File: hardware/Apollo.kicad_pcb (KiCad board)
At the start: 2 copper layers, 101.2 x 199.1 mm, 82 parts, among them J1 TYPE-C 16PIN 2MD(073), J2 Conn_ARM_JTAG_SWD_10, J22 Conn_01x16, J3 Conn_02x03_Odd_Even, J4 Conn_02x04_Odd_Even, Q1 DMP1045U-7, Q2 SS8550, Q3 SS8050, Q4 SS8050, Q5 SL1254-3, SW1 MK-12C01-G1.5, SW2 TS-1095PS-A1B2-C3D2, SW3 TS-1095PS-A1B2-C3D2, SW4 10*10*9-6P WX, U1 TPS63031DSK, U10 PY25Q128HA, U11 SAINTCON-Minibadge, U12 SAINTCON-Minibadge, U2 RP2350A-QFN60, U3 SAINTCON-Minibadge, U4 SAINTCON-Minibadge, U5 SAINTCON-Minibadge, U6 SAINTCON-Minibadge, U7 24CS02, U8 SAINTCON-Minibadge, U9 SAINTCON-Minibadge, Y1 12Mhz

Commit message: prototype v0.3
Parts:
- removed SW4: 10*10*9-6P WX, easyeda2kicad:SW-SMD-6P-L10.5-W10.0_C2858290
- added SW5: 7*7*5-6P-L WX, easyeda2kicad:SW-SMD_8P-L7.0-W7.0-P1.40-LS7.4-TL, F.Cu at (112.7, 172.2)
- added TP4: TestPoint, TestPoint:TestPoint_Pad_D1.0mm, B.Cu at (166.6, 173.2)
- added TP5: TestPoint, TestPoint:TestPoint_Pad_D1.0mm, B.Cu at (122.0, 173.0)
- C14: value 0.1uF -> 100nF
- moved TP2 13.2 mm to (176.6, 168.0)
- moved TP1 13.2 mm to (174.0, 168.0)
- moved TP3 13.2 mm to (171.4, 168.0)
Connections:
- U2 pad 31: JOY_B -> JOY_L
- U2 pad 33: JOY_U -> JOY_B
- U2 pad 35: JOY_L -> JOY_U
- U2 pad 43: unconnected-(U2-GPIO29_ADC3-Pad43) -> Net-(U2-GPIO29_ADC3)
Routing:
- net Net-(U2-GPIO29_ADC3): track 0.00 -> 91.3 mm, vias 0 -> 2
- net +3.3V: track 841.1 -> 805.7 mm
- net JOY_D: track 104.8 -> 96.8 mm
- net TX: track 170.9 -> 174.1 mm
- net JOY_B: track 93.1 -> 96.0 mm
- net Net-(D5-DOUT): track 47.7 -> 50.1 mm
- net JOY_U: track 101.2 -> 99.1 mm
- net BTN2: track 121.7 -> 120.3 mm
- net Net-(D7-DOUT): track 49.8 -> 48.4 mm
- net JOY_R: track 96.0 -> 94.9 mm
- net 1HZ_CLK: track 201.6 -> 202.3 mm
- net SCL: track 225.6 -> 226.1 mm
- net SDA: track 225.8 -> 226.3 mm
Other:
- board text removed: "SAINTCON"

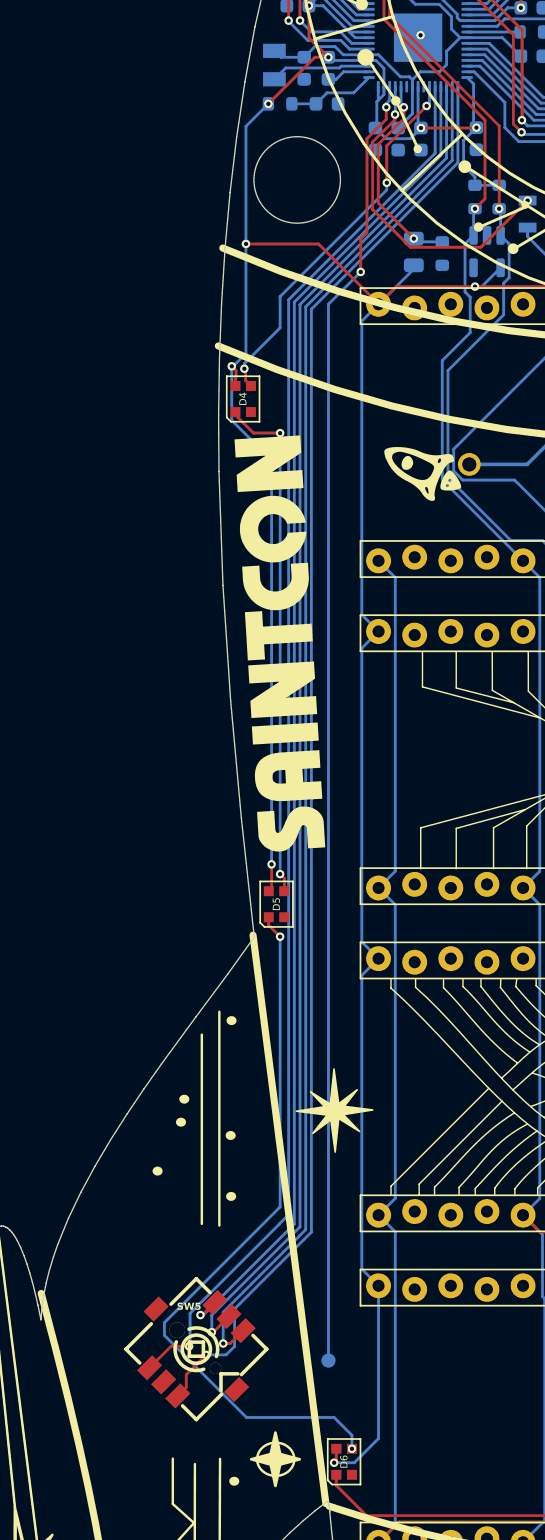
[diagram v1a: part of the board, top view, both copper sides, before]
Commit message: Updated joystick
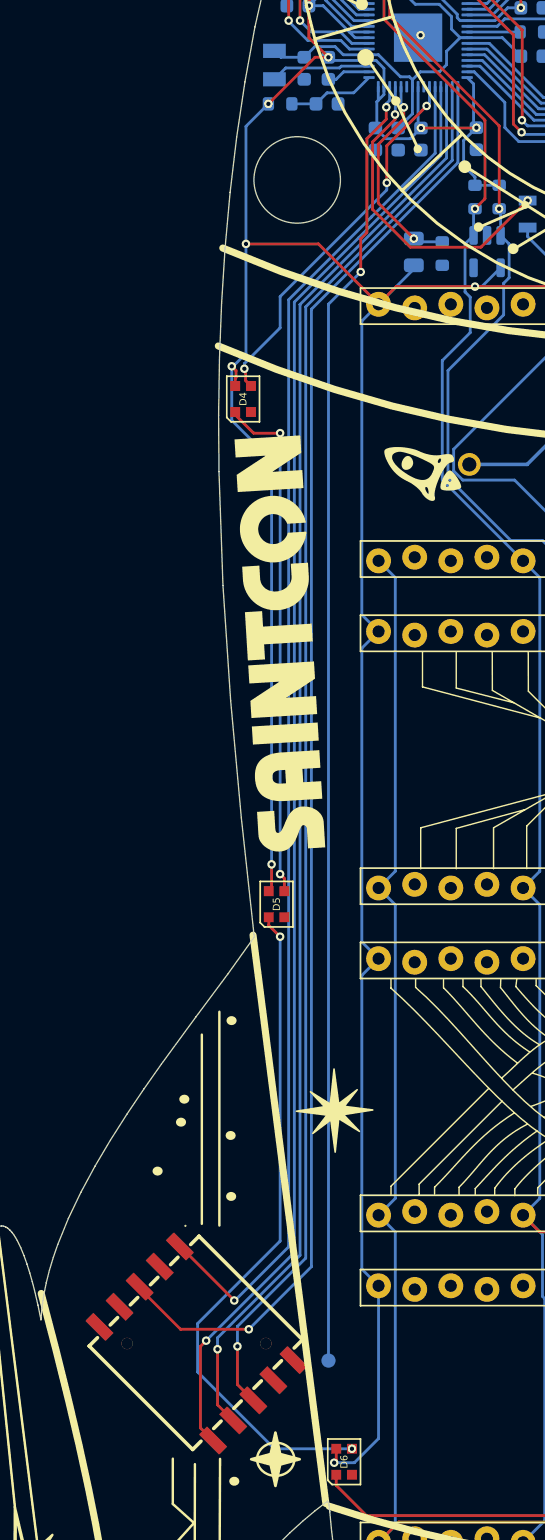
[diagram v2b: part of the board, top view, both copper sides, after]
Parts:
- removed SW5: 7*7*5-6P-L WX, easyeda2kicad:SW-SMD_8P-L7.0-W7.0-P1.40-LS7.4-TL
- added SW4: K1-1507SA-03, easyeda2kicad:KEY-SMD_K1-1507SA-03, F.Cu at (112.7, 171.8)
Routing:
- net JOY_R: track 94.9 -> 102.5 mm
- net JOY_B: track 96.0 -> 100.9 mm
- net JOY_U: track 99.1 -> 96.6 mm
- net Net-(D5-DOUT): track 50.1 -> 47.8 mm
- net JOY_D: track 96.8 -> 99.1 mm
- net JOY_L: track 101.0 -> 102.4 mm

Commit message: accel added
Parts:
- added C23: 1uF, Capacitor_SMD:C_0603_1608Metric, B.Cu at (139.0, 89.4)
- added C24: 100nF, Capacitor_SMD:C_0603_1608Metric, B.Cu at (140.8, 89.4)
- added U13: STK8321, Package_LGA:LGA-12_2x2mm_P0.5mm, B.Cu at (136.4, 89.2)
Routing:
- net +3.3V: track 805.7 -> 821.5 mm, vias 24 -> 27
- net SCL: track 226.1 -> 231.1 mm
- net GND: track 18.4 -> 20.3 mm, vias 5 -> 7
- net SDA: track 226.3 -> 228.0 mm, vias 2 -> 3

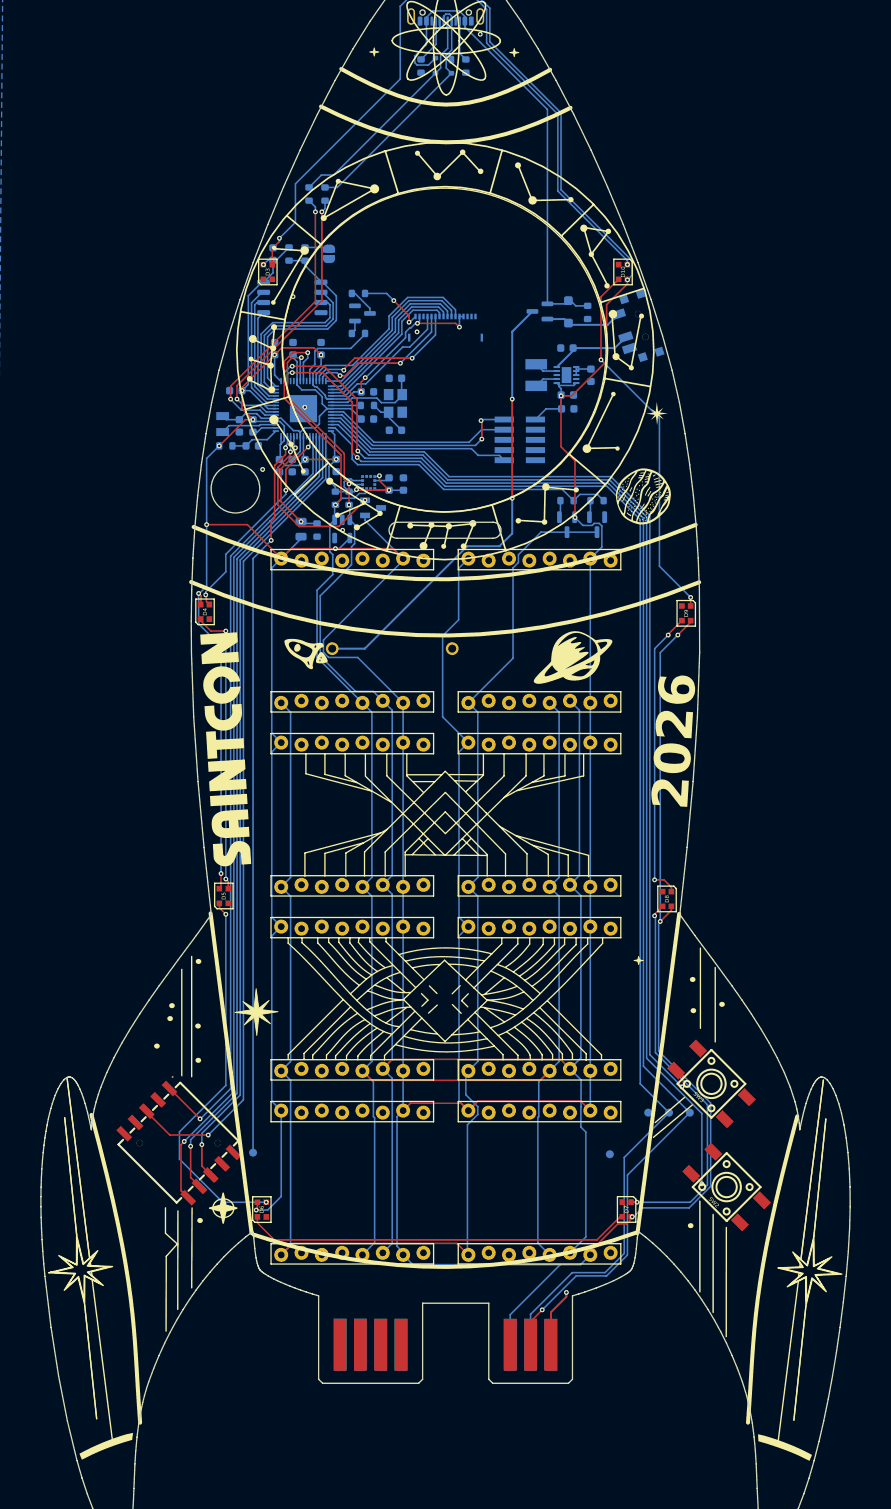
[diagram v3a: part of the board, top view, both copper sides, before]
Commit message: Restoring Orion trail
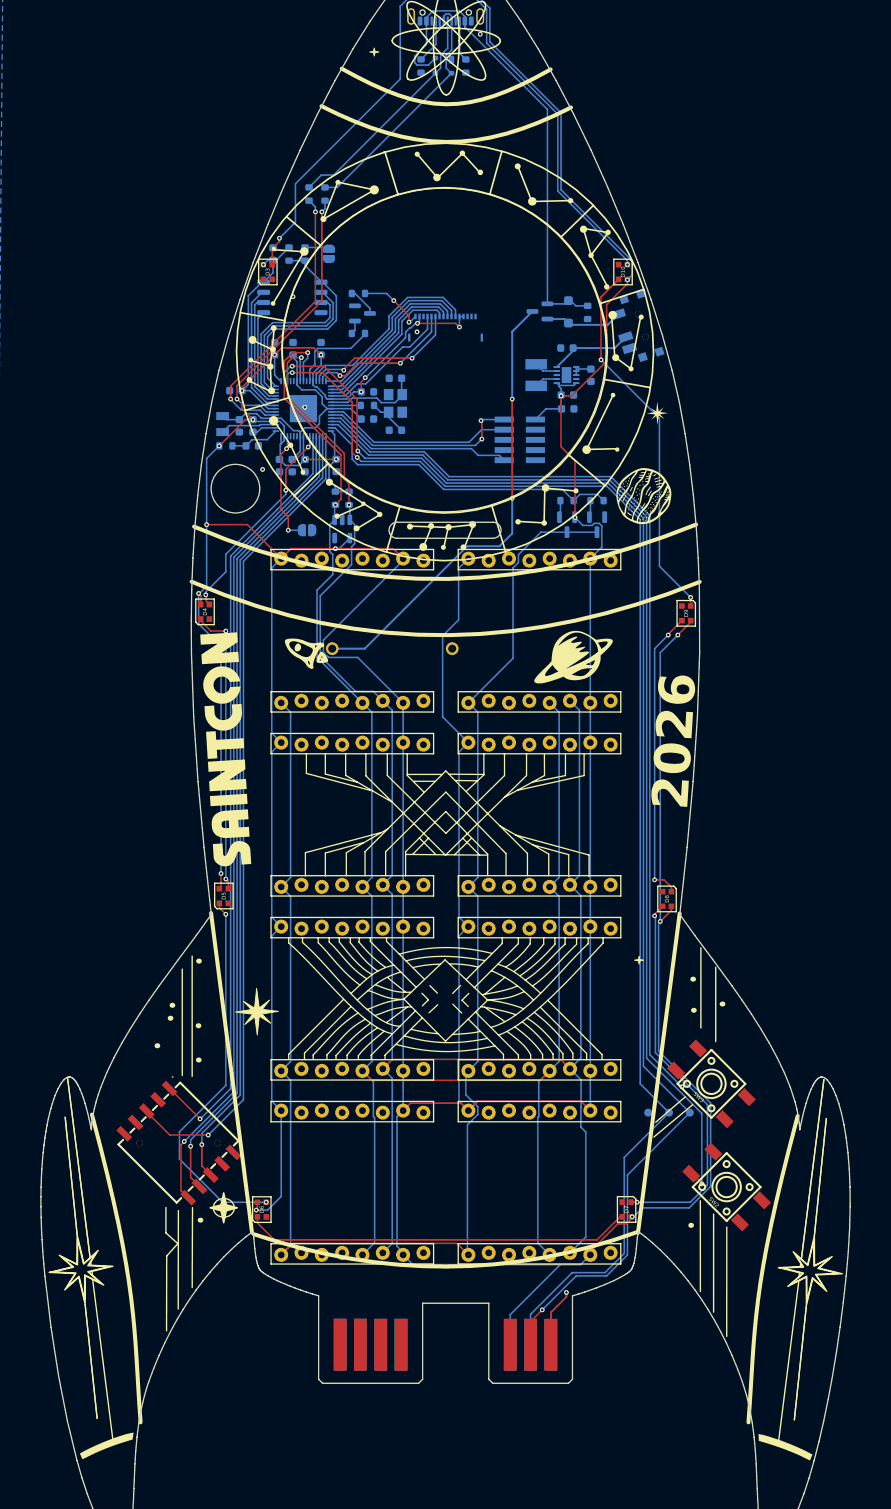
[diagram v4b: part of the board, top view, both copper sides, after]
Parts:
- removed C23: 1uF, Capacitor_SMD:C_0603_1608Metric
- removed C24: 100nF, Capacitor_SMD:C_0603_1608Metric
- removed Q5: SL1254-3, easyeda2kicad:SOT-23-3_L2.9-W1.3-P1.90-LS2.4-BR
- removed R18: 1K, Resistor_SMD:R_0603_1608Metric
- removed R4: PT0805, LED_SMD:LED_0805_2012Metric
- removed TP4, TP5: TestPoint, TestPoint:TestPoint_Pad_D1.0mm
- removed U13: STK8321, Package_LGA:LGA-12_2x2mm_P0.5mm
- added Solo: Jumper_2_Open, Jumper:SolderJumper-2_P1.3mm_Open_RoundedPad1.0x1.5mm, B.Cu at (128.8, 95.2)
- renumbered JP1 to Boot
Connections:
- U2 pad 41: LIGHT -> unconnected-(U2-GPIO27_ADC1-Pad41)
- U2 pad 42: HALL -> unconnected-(U2-GPIO28_ADC2-Pad42)
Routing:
- net Net-(JP2-B): track 91.3 -> 14.2 mm
- net +3.3V: track 821.5 -> 794.6 mm, vias 27 -> 24
- net HALL: track 22.7 -> 0.00 mm, vias 2 -> 0
- net LIGHT: track 14.6 -> 0.00 mm, vias 2 -> 0
- net SCL: track 231.1 -> 226.1 mm
- net GND: track 20.3 -> 18.4 mm, vias 7 -> 6
- net SDA: track 228.0 -> 226.3 mm, vias 3 -> 2
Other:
- board text added: "JLC JLC JLC"
